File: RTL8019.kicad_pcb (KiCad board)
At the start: 2 copper layers, 104.1 x 73.2 mm, 56 parts, among them J1 ROM_0, J10 IRQ_2, J11 IO_0, J12 IO_1, J13 IO_2, J14 IO_3, J2 ROM_1, J3 ROM_2, J4 ROM_3, J5 ROM_4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

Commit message: Add files via upload
Added info string to pcb
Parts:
- removed G*** (x2): LOGO, owl:owl-20mm
- added REF**: owl-20mm-mask, owl:owl-20mm-mask, B.Cu at (200.1, 62.2)
- added REF**: owl-20mm-mask-base, owl:owl-20mm-mask-base, B.Cu at (200.1, 62.2)
- added REF**: owl-20mm-mask, owl:owl-20mm-mask, F.Cu at (200.0, 62.2)
- added REF**: owl-20mm-mask-base, owl:owl-20mm-mask-base, F.Cu at (200.0, 62.2)
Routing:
- net GND: vias 138 -> 130
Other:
- board text added: "Chanterelle"
- board text added: "RTETH-XT-A1 rev 0.9"
- board text removed: "J1-J5 - ROM configuration: 0 0 * * * Disabled 0 1 0 0 0 C000h, 32K 0 1 0 0 1 C800h, 32K 0 1 0 1 0 D000h, 32K 0 1 0 1 1 D800h, 32K 0 1 1 0 0 C000h, 64K 0 1 1 0 1 D000h, 64K 1 0 0 0 0 C000h, 16K 1 0 0 0 1 C400h, 16K 1 0 0 1 0 C800h, 16K 1 0 0 1 1 CC00h, 16K 1 0 1 0 0 D000h, 16K 1 0 1 0 1 D400h, 16K 1 0 1 1 0 D800h, 16K 1 0 1 1 1 DC00h, 16K 1 1 0 0 0 C000h, Page 1 1 0 0 1 C400h, Page 1 1 0 1 0 C800h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"
- board text removed: "J11-J14 - I/O Select 0 0 0 0 - 300H 0 0 0 1 - 320H 0 0 1 0 - 340H 0 1 0 0 - 360H 1 0 0 0 - 380H 1 0 0 1 - 3A0H 1 0 1 0 - 3C0H 1 0 1 1 - 3E0H 0 1 0 0 - 200H 0 1 0 1 - 220H 0 1 1 0 - 240H 0 1 1 1 - 260H 1 1 0 0 - 280H 1 1 0 1 - 2A0H 1 1 1 0 - 2C0H 1 1 1 1 - 2E0H"

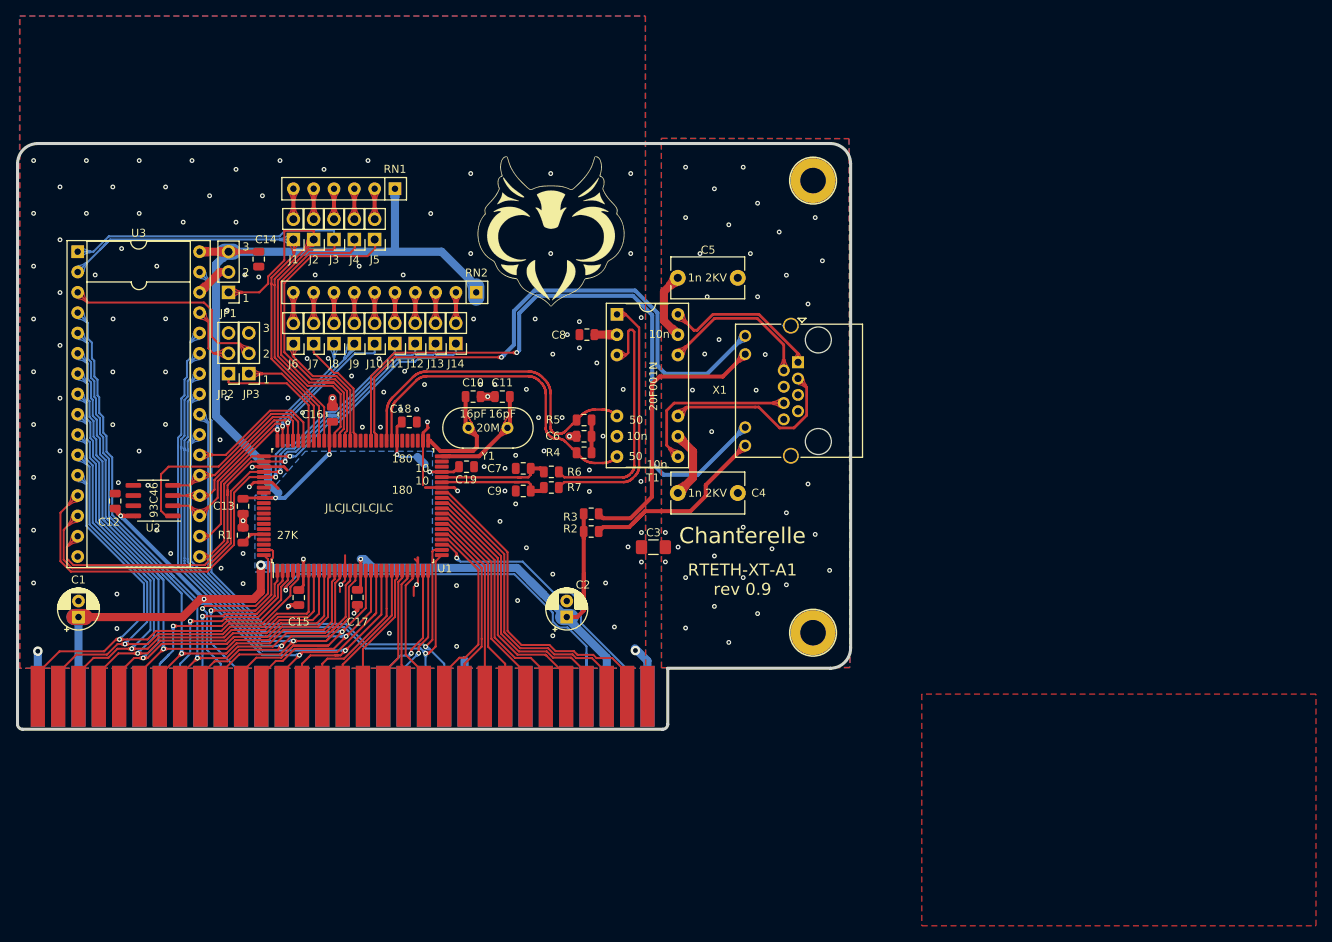
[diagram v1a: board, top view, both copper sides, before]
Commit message: Add files via upload
Fixed - incorrect rtl8019as footprint
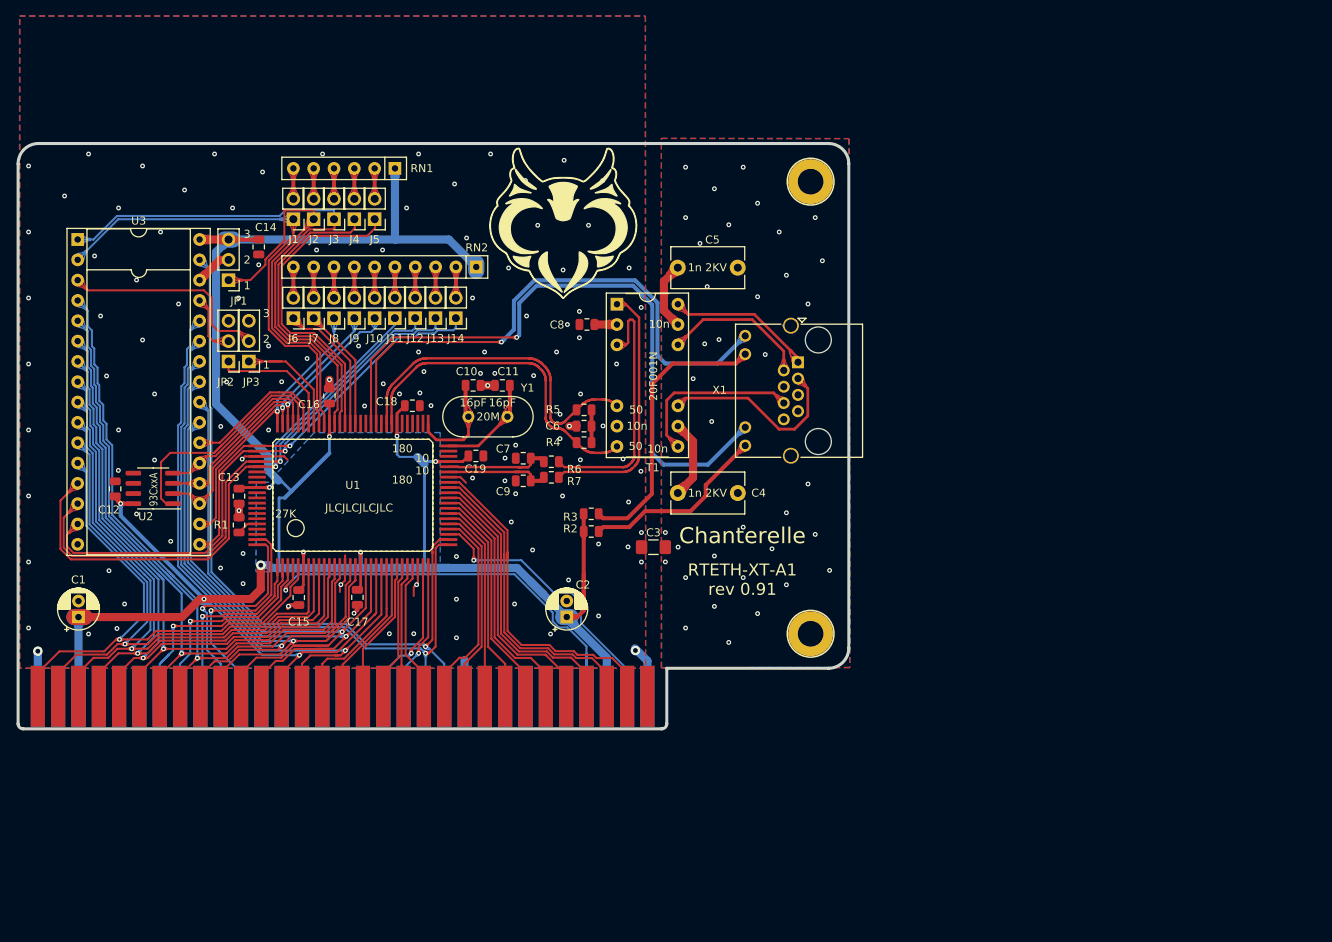
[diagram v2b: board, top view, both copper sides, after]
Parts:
- removed the REF** at (200.1, 62.2) (x2)
- removed the REF** at (200.0, 62.2) (x2)
- added REF**: owl-20mm-mask, owl:owl-20mm-mask, B.Cu at (201.6, 61.2)
- added REF**: owl-20mm-mask-base, owl:owl-20mm-mask-base, B.Cu at (201.6, 61.2)
- added REF**: owl-20mm-mask-base, owl:owl-20mm-mask-base, F.Cu at (201.5, 61.2)
- added REF**: owl-20mm-mask, owl:owl-20mm-mask, F.Cu at (201.5, 61.2)
- R2, R3: value 220 -> 510
- U1: footprint Package_QFP:PQFP-100_14x20mm_P0.65mm -> 20f001ng:8019as
- U2: value 93C46 -> 93CxxA
- moved J10 3.17 mm to (178.0, 73.1)
- moved J11 3.17 mm to (180.5, 73.1)
- moved J12 3.17 mm to (183.1, 73.1)
- moved J13 3.17 mm to (185.6, 73.1)
- moved J14 3.17 mm to (188.1, 73.1)
- moved J6 3.17 mm to (167.8, 73.1)
- moved J7 3.17 mm to (170.4, 73.1)
- moved J8 3.17 mm to (172.9, 73.1)
- moved J9 3.17 mm to (175.5, 73.1)
- moved RN2 3.17 mm to (190.7, 66.7)
- moved J1 2.54 mm to (167.8, 60.7)
- moved J2 2.54 mm to (170.4, 60.7)
- moved J3 2.54 mm to (172.9, 60.7)
- moved J4 2.54 mm to (175.5, 60.7)
- moved J5 2.54 mm to (178.0, 60.7)
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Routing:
- net VCC: track 272.5 -> 306.6 mm
- net GND: track 57.3 -> 45.4 mm, vias 130 -> 120
- net RE: track 71.0 -> 75.4 mm
- net SD6: track 41.3 -> 45.0 mm
- net WE: track 90.4 -> 93.8 mm
- net Net-(R2-Pad1): track 26.5 -> 23.6 mm
- net BA17: track 47.5 -> 50.1 mm
- net IRQ6: track 26.4 -> 28.7 mm
- net SD7: track 41.2 -> 43.2 mm
- net BA19: track 39.5 -> 37.5 mm
- net BD4: track 33.9 -> 35.6 mm
- net SA9: track 74.6 -> 76.4 mm
- net LED_LINK: track 71.5 -> 69.9 mm
- net IRQ7: track 27.6 -> 29.2 mm
- net Net-(U1-Pad76): track 29.7 -> 31.2 mm
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- removed copper zone on F.Cu, net VCC
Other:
- board size 104.1 x 73.2 mm -> 103.8 x 73.2 mm
- net class eth added: clearance 0.15, trace_width 0.1524, via_dia 0.6, via_drill 0.3
- board text added: "J11-J14 I/O Select 0 0 0 0 - 300H 0 0 0 1 - 320H 0 0 1 0 - 340H 0 1 0 0 - 360H 1 0 0 0 - 380H 1 0 0 1 - 3A0H 1 0 1 0 - 3C0H 1 0 1 1 - 3E0H"
- board text added: "J8-J10 - IRQ Select 0 0 0 - IRQ2 0 0 1 - IRQ3 0 1 0 - IRQ4 0 1 1 - IRQ5 1 0 0 - IRQ6* 1 0 1 - IRQ7*"
- board text added: "RTETH-XT-A1 rev 0.91"
- board text removed: "J11-J14 - I/O Select 0 0 0 0 - 300H 0 0 0 1 - 320H 0 0 1 0 - 340H 0 1 0 0 - 360H 1 0 0 0 - 380H 1 0 0 1 - 3A0H 1 0 1 0 - 3C0H 1 0 1 1 - 3E0H"
- board text removed: "J8-J10 - IRQ Select 0 0 0 - IRQ2 0 0 1 - IRQ3 0 1 0 - IRQ4 0 1 1 - IRQ5 1 0 0 - IRQ6 1 0 1 - IRQ7"
- board text removed: "RTETH-XT-A1 rev 0.9"
